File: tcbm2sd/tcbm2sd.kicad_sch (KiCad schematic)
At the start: 30 parts, among them J1 TCBM, J2 JTAG, J3 GPIO, J4 AMS1117, J5 SD CARD, J7 ALT_A6_A7, SW1 BUT_PREV, SW2 BUT_NEXT, U1 XC9572XL-VQ64, U2 Arduino Pro Mini, U3 AMS1117-3.3, U4 27C512, U5 74HC00

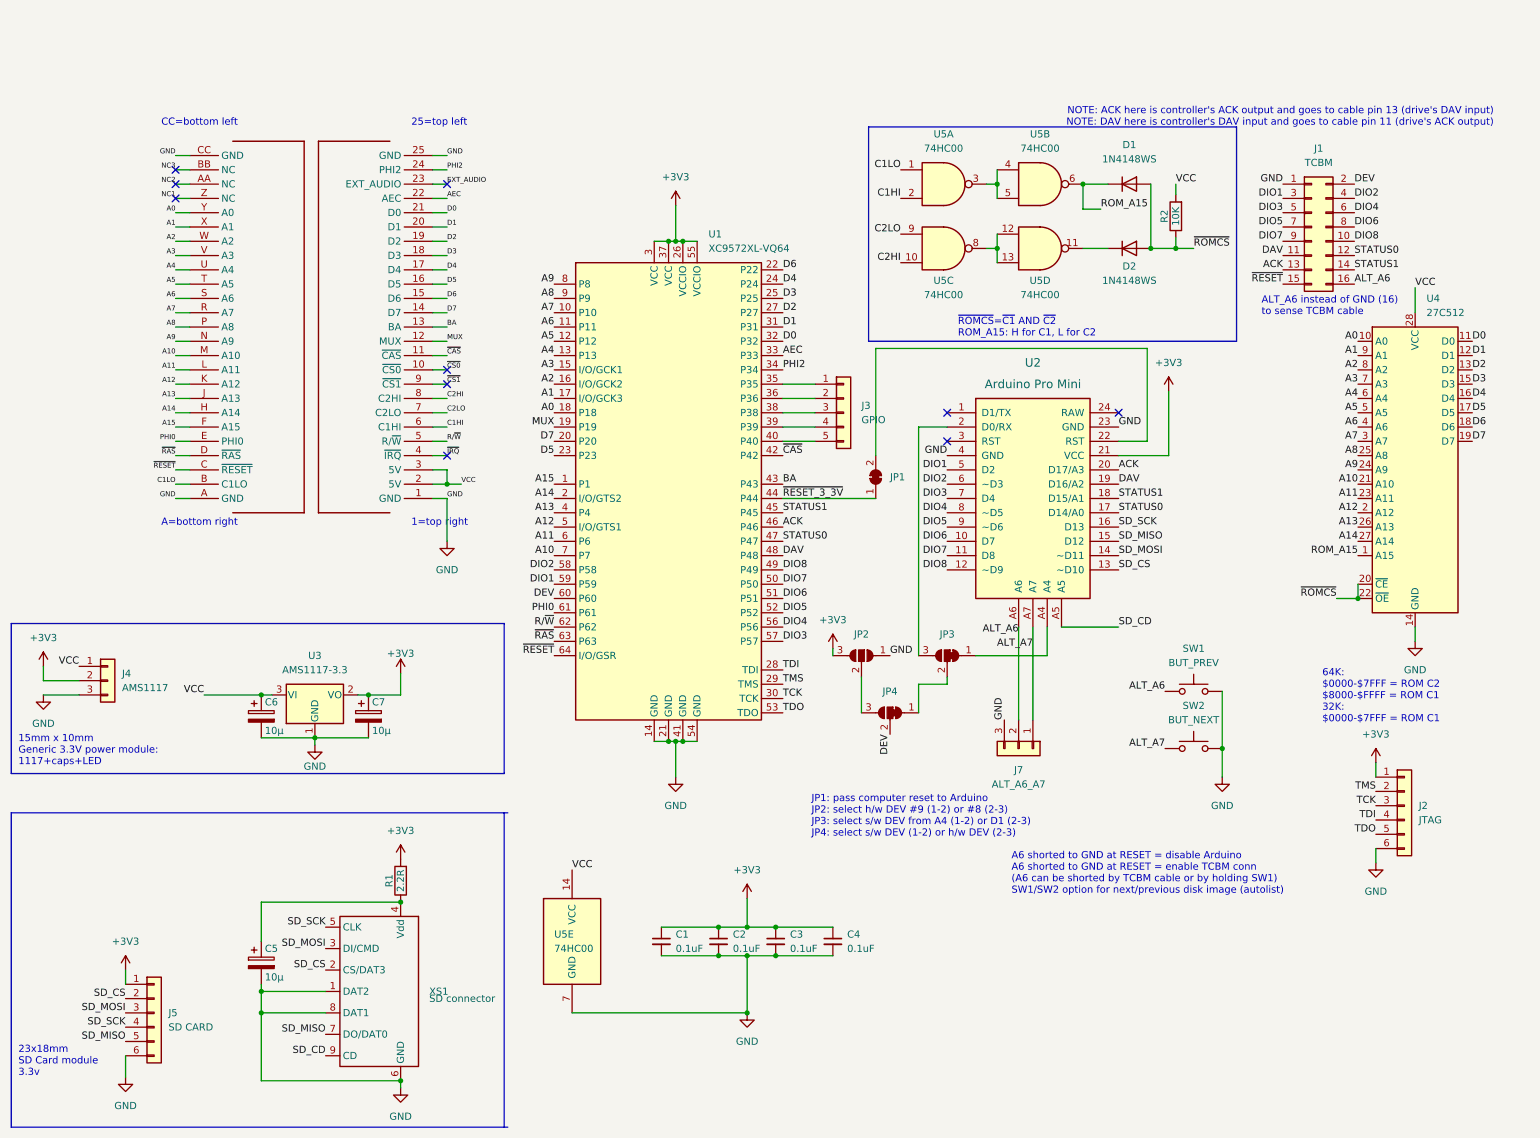
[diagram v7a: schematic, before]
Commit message: remove GPIO connector, 74'00, diodes and pullup; added pullups for A6/A7; JP1 (reset passthrough) default open; bump revision to 1.3
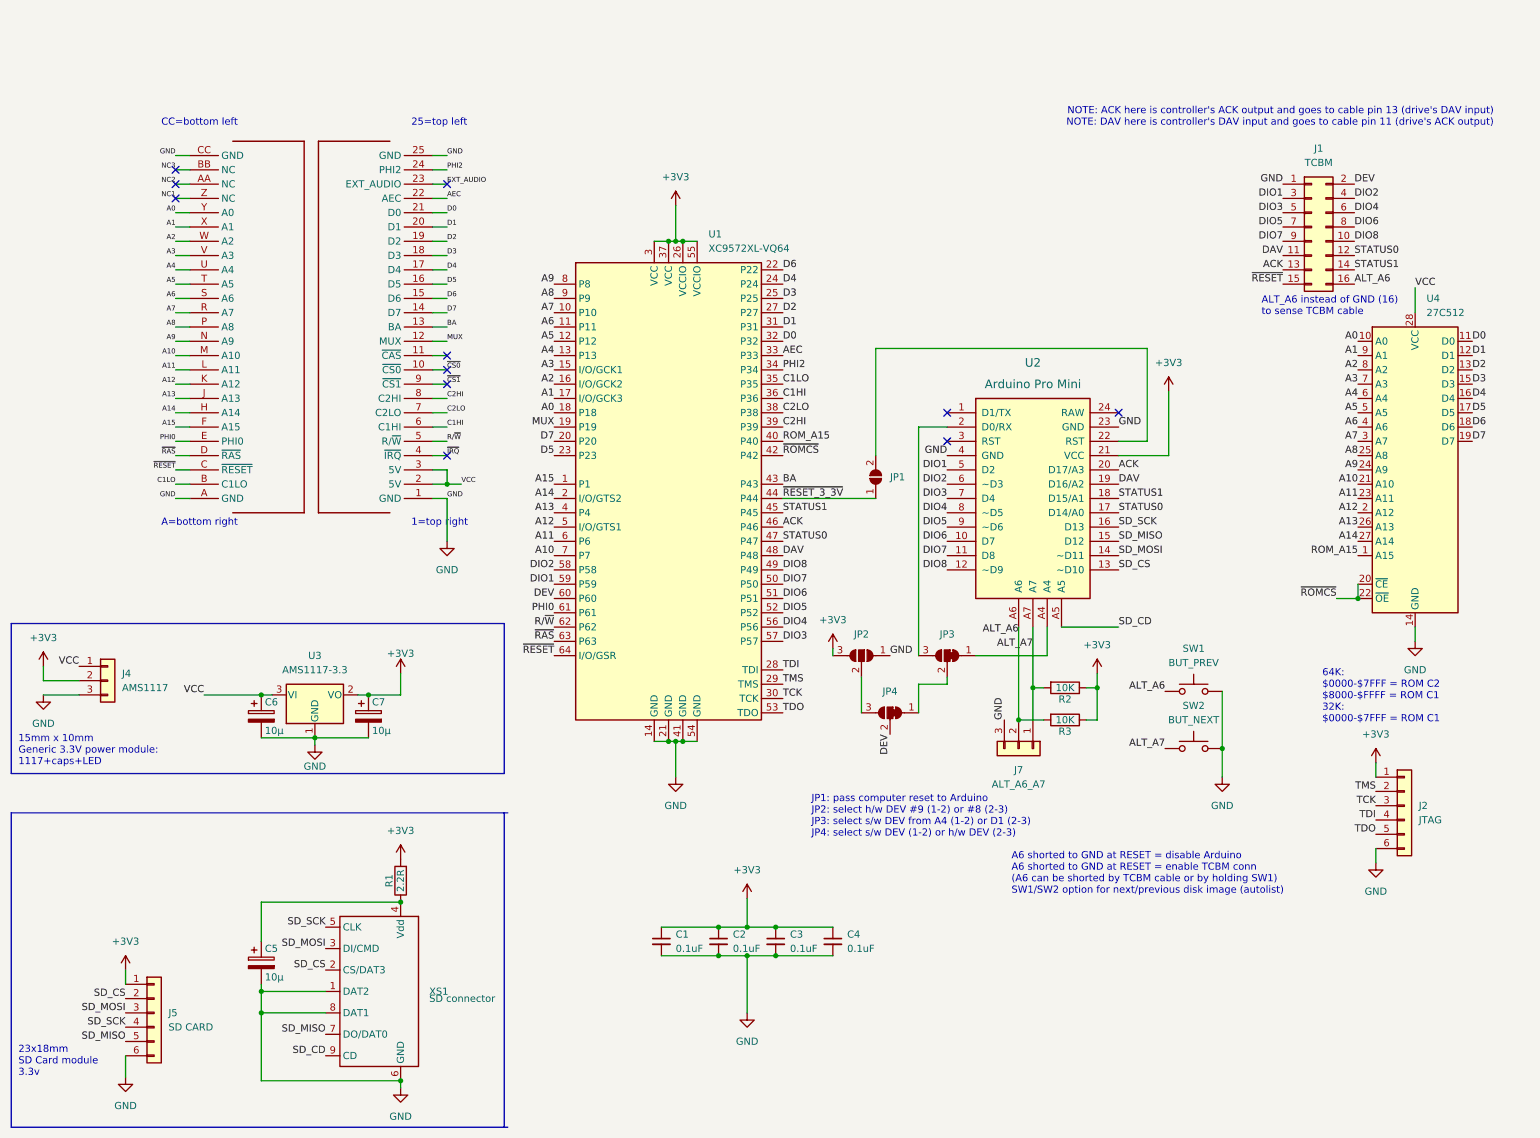
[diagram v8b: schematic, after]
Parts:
- removed D1, D2: 1N4148WS, Diode_SMD:D_SOD-323, symbol Diode:1N4148WS
- removed J3: GPIO, Connector_PinHeader_2.54mm:PinHeader_1x05_P2.54mm_Vertical, symbol Connector_Generic:Conn_01x05
- removed JP1: SolderJumper_2_Bridged, Jumper:SolderJumper-2_P1.3mm_Bridged_Pad1.0x1.5mm, symbol Jumper:SolderJumper_2_Bridged
- removed U5: 74HC00, Package_SO:SO-14_3.9x8.65mm_P1.27mm, symbol 74xx:74HC00
- added JP1: SolderJumper_2_Open, Jumper:SolderJumper-2_P1.3mm_Open_Pad1.0x1.5mm, symbol Jumper:SolderJumper_2_Open
- added R3: 10K, Resistor_SMD:R_0805_2012Metric_Pad1.20x1.40mm_HandSolder, symbol Device:R
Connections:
- net +3V3: now also R2.1, R3.1
- net ALT_A6: now also R3.2
- net ALT_A7: now also R2.2
- net C1HI: now also U1.36 (P36)
- net C1LO: now also U1.35 (P35)
- net C2HI: now also U1.39 (P39)
- net C2LO: now also U1.38 (P38)
- net ROM_A15: now also U1.40 (P40)
- net VCC: no longer R2.2
- net ~{RESET_3_3V}: now also JP1.1 (A)
- net ~{ROMCS}: now also U1.42 (P42); no longer R2.1
- net at U2.22 (RST): now also JP1.2 (B)
- net ~{CAS}: no longer names the net of U$1.11 (~{CAS})
- net ~{CAS}: no longer U1.42 (P42)
- no-connect marks 10 -> 11
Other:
- note removed: "~{ROMCS}=~{C1} AND ~{C2} ROM_A15: H for C1, L for C2"
